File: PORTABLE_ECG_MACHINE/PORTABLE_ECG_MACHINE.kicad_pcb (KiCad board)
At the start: 2 copper layers, 25.5 x 64.8 mm, 83 parts, among them IC1 AD8232ACPZ, J1 UART, J2 AudioJack3, J3 Li-Ion 3.7 CONN, J4 USB_C_Receptacle_USB2.0, Q1 BSS138, Q2 BSS138, SW1 SW_SPDT, U1 SSD1306, U2 CP2102-GM, U3 ATmega328PB-A, U4 TC1262-33, U5 TP4056, Y1 16MHZ

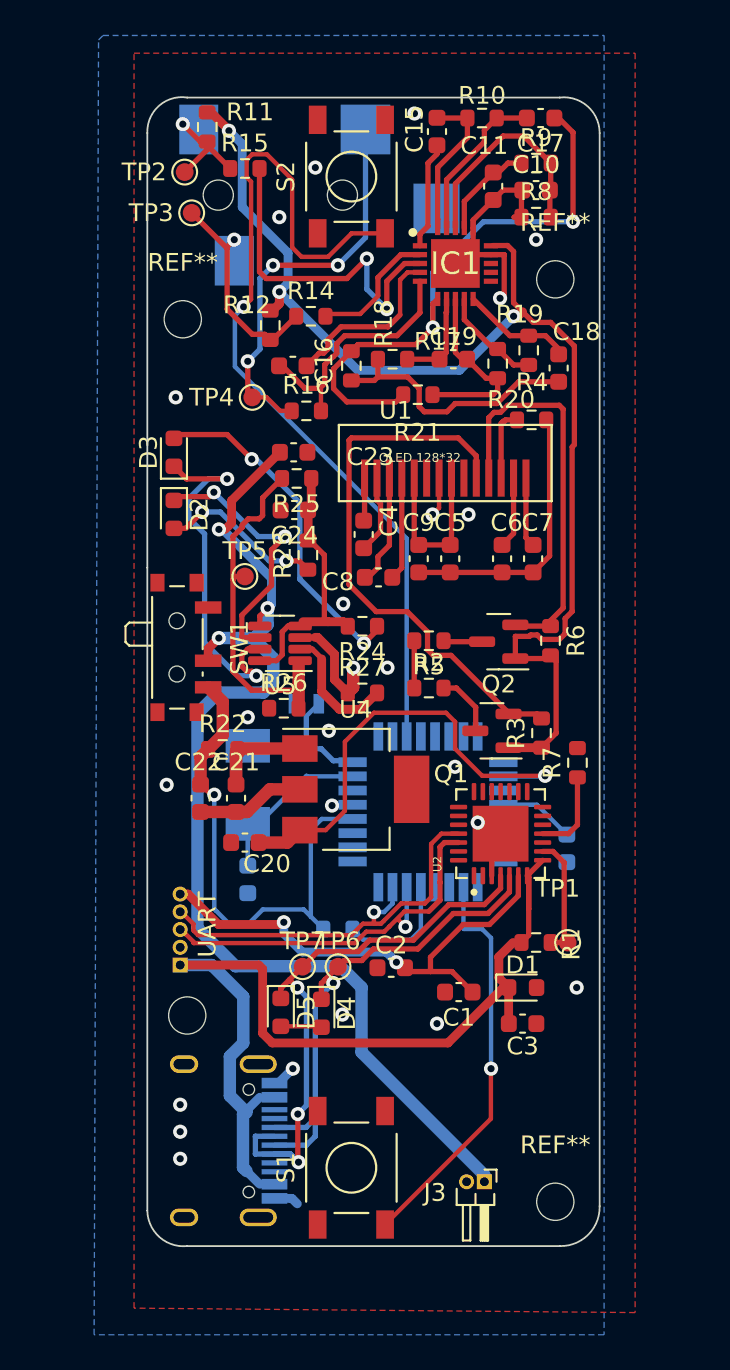
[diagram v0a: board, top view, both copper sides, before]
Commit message: F.SILK AND B.SILK -- FONT FIX | LAYOUT FIX
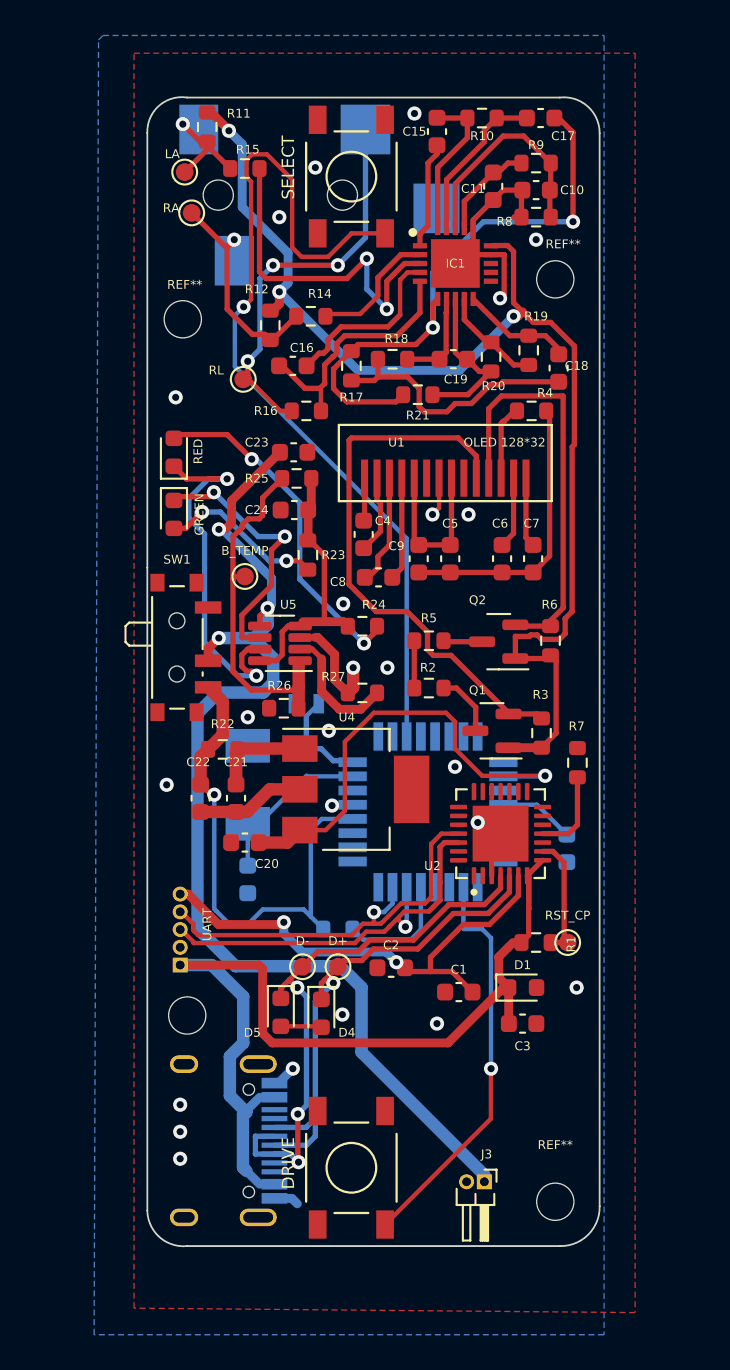
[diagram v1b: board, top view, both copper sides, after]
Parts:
- moved RL 1.14 mm to (89.4, 40.4)
- moved R20 0.53 mm to (103.4, 39.1)
- moved R4 0.51 mm to (105.7, 42.2)
- renumbered TP5 to B_TEMP, TP6 to D+, TP7 to D-, S1 to DRIVE, D2 to GREEN, TP2 to LA, TP3 to RA, D3 to RED, TP4 to RL, TP1 to RST_CP, S2 to SELECT
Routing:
- net SDA_3.3: track 22.4 -> 23.6 mm
- net /REF_OUT: track 10.5 -> 9.35 mm
- net GND: track 54.8 -> 55.3 mm
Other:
- board text added: "*"
- board text added: "+"
- board text added: "-"
- board text added: "AMIT TONY JOSEPH"
- board text added: "ARUN JYOTHISH"
- board text added: "ATMEGA328PB-A"
- board text added: "BAT 3.7"
- board text added: "BHARATH SRINIVAS"
- board text added: "GOURI KRISHNA"
- board text added: "GROUP NO. 5"
- board text added: "TEAM MEMBERS"

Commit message: CUSTOM PAD ADD | ANNOTATION CONFLICT RECTIFY
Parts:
- added J5: Conn_01x06_Male, TEST_POINT_MATRIX_6-PIN:6PIN_CONN, B.Cu at (104.9, 59.7)
- renumbered B_TEMP to B_TEMP1, D+ to D+1, D- to D-1, D4 to D2, D5 to D3, DRIVE to DRIVE1, GREEN to GREEN1, LA to LA1, R13 to R11, R11 to R12, R12 to R13, RA to RA1, RED to RED1, RL to RL1, RST_CP to RST_CP1, SELECT to SELECT1
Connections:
- U3 pad 12: unconnected-(U3-Pad12) -> Net-(U3-Pad12)
- U3 pad 13: unconnected-(U3-Pad13) -> Net-(U3-Pad13)
- U3 pad 14: unconnected-(U3-Pad14) -> Net-(U3-Pad14)
- U3 pad 15: unconnected-(U3-Pad15) -> Net-(U3-Pad15)
- U3 pad 16: unconnected-(U3-Pad16) -> Net-(U3-Pad16)
- U3 pad 17: unconnected-(U3-Pad17) -> Net-(U3-Pad17)
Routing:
- net Net-(U3-Pad13): track 0.00 -> 11.7 mm
- net Net-(U3-Pad12): track 0.00 -> 11.3 mm
- net Net-(U3-Pad15): track 0.00 -> 9.41 mm
- net Net-(U3-Pad14): track 0.00 -> 9.01 mm
- net Net-(U3-Pad17): track 0.00 -> 7.08 mm
- net Net-(U3-Pad16): track 0.00 -> 6.76 mm

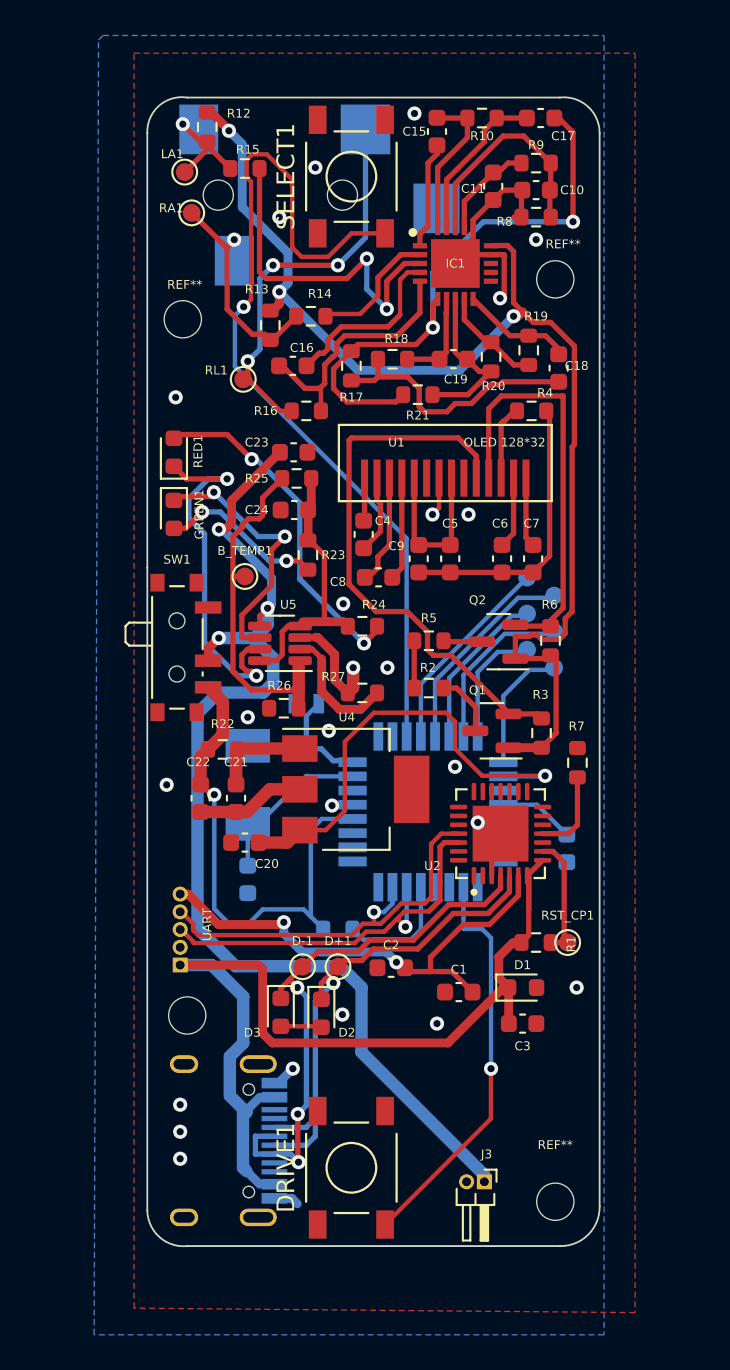
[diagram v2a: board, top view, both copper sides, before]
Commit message: conn complete | solder jumper add
pcbnew connection complete with respect to schematics, solder jumper add
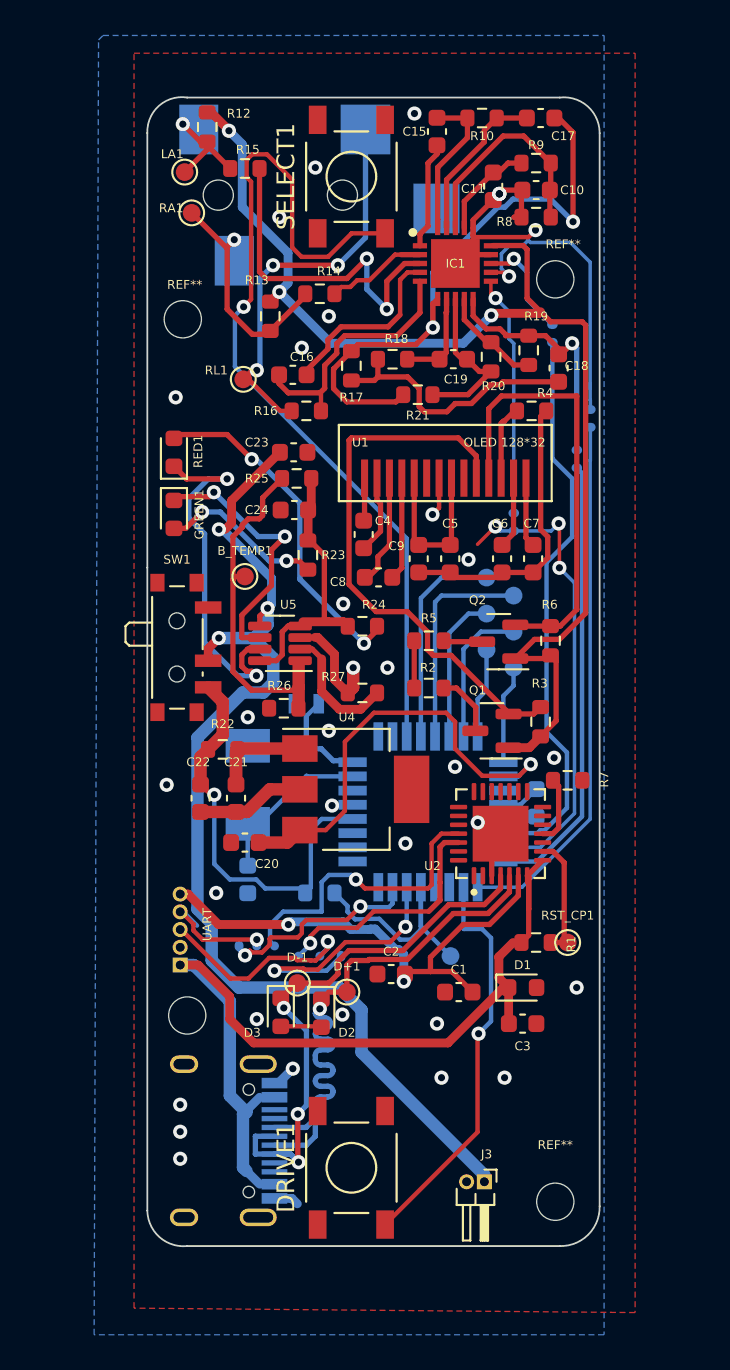
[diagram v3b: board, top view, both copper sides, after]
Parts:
- added JP1: SolderJumper_3_Open, TEST_POINT_MATRIX_6-PIN:3_PIN_SOLDER_JUMPER_SMD, B.Cu at (94.3, 70.3)
- added JP2: SolderJumper_3_Open, TEST_POINT_MATRIX_6-PIN:3_PIN_SOLDER_JUMPER_SMD, B.Cu at (89.6, 74.9)
- added JP3: LDO+, TEST_POINT_MATRIX_6-PIN:2_PIN_SMD_SOLDER_JUMPER, B.Cu at (112.8, 43.7)
- added JP4: LDO-, TEST_POINT_MATRIX_6-PIN:2_PIN_SMD_SOLDER_JUMPER, B.Cu at (108.5, 49.5)
- added JP5: OUT, TEST_POINT_MATRIX_6-PIN:2_PIN_SMD_SOLDER_JUMPER, B.Cu at (112.0, 46.0)
- added JP6: LDO+, TEST_POINT_MATRIX_6-PIN:2_PIN_SMD_SOLDER_JUMPER, B.Cu at (110.6, 38.9)
- added TP1: AT_RST#, TestPoint:TestPoint_Pad_D1.0mm, B.Cu at (101.1, 72.9)
- moved C12 3.10 mm to (105.9, 64.3)
- moved J5 2.29 mm to (102.6, 59.7)
- moved R11 2.27 mm to (93.7, 69.3)
- moved D+1 1.51 mm to (95.2, 74.9)
- moved R14 1.37 mm to (93.7, 35.6)
- moved R7 1.14 mm to (107.7, 63.0), turned to 0 degrees
- moved D-1 0.97 mm to (92.5, 74.4)
- moved R3 0.64 mm to (106.2, 59.7)
- moved R13 0.51 mm to (90.9, 36.8)
- moved C16 0.51 mm to (92.2, 40.1)
- moved C2 0.36 mm to (97.7, 73.9)
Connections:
- net Net-(C18-Pad1) renamed /OUT
- IC1 pad 11: /LDO- -> /LOD-
- IC1 pad 12: /LDO+ -> /LOD+
- J1 pad 3: /TXD -> Net-(J1-Pad3)
- J1 pad 4: /RXD -> Net-(J1-Pad4)
- U2 pad 25: /RXD -> /CP_RXD
- U2 pad 26: /TXD -> /CP_TXD
- U3 pad 22: unconnected-(U3-Pad22) -> /AT_SDN#
- U3 pad 23: unconnected-(U3-Pad23) -> /AT_LOD-
- U3 pad 24: unconnected-(U3-Pad24) -> /AT_ADC1
- U3 pad 25: unconnected-(U3-Pad25) -> /AT_LOD+
- U3 pad 30: /TXD -> /AT_RXD
- U3 pad 31: /RXD -> /AT_TXD
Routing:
- net /AT_SDN#: track 0.00 -> 32.0 mm
- net /AT_LOD+: track 0.00 -> 30.0 mm
- net /AT_LOD-: track 0.00 -> 26.8 mm, vias 0 -> 3
- net /AT_ADC1: track 0.00 -> 25.3 mm
- net /RXD: track 23.4 -> 0.00 mm, vias 1 -> 0
- net /TXD: track 23.0 -> 0.00 mm, vias 1 -> 0
- net /CP_RXD: track 0.00 -> 17.0 mm, vias 0 -> 1
- net /LOD+: track 0.00 -> 17.0 mm, vias 0 -> 1
- net /AT_RXD: track 0.00 -> 14.8 mm, vias 0 -> 2
- net /CP_TXD: track 0.00 -> 13.7 mm, vias 0 -> 1
- net /LOD-: track 0.00 -> 13.6 mm, vias 0 -> 1
- net Net-(J1-Pad3): track 0.00 -> 11.7 mm, vias 0 -> 1
- net /AT_TXD: track 0.00 -> 11.6 mm, vias 0 -> 2
- net /OUT: track 6.29 -> 14.0 mm, vias 0 -> 1
- net Net-(J1-Pad4): track 0.00 -> 6.81 mm, vias 0 -> 1
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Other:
- board text added: "MISO"
- board text added: "MOSI"
- board text added: "PB0"
- board text added: "PB1"
- board text added: "PB2"
- board text added: "SCK"

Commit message: new revision initiate
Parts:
- moved R7 1.78 mm to (107.7, 61.2), turned to 90 degrees
- moved D2 1.14 mm to (93.5, 77.2)
- moved R3 1.02 mm to (106.2, 58.7)
- moved D-1 0.76 mm to (93.2, 74.4)
- moved D3 0.38 mm to (91.5, 76.5)
- moved C19 0.16 mm to (101.1, 39.2)
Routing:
- net GND: track 58.2 -> 77.9 mm
- net VIN: track 52.8 -> 58.0 mm
- net /AT_LOD-: track 26.8 -> 24.2 mm, vias 3 -> 2
- net Net-(R7-Pad1): track 3.85 -> 4.88 mm
- net 3.3V: track 68.9 -> 68.3 mm

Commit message: git pull stash?
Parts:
- added REF**: SSD1306-128*64, user_ftprint:SSD1306-128*64, F.Cu at (91.9, 78.5)
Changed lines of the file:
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@@
     )
+  )
+  (footprint "user_ftprint:SSD1306-128*64" (layer "F.Cu")
+    (at 91.948 78.486)
+    (attr smd)
+    (fp_text reference "REF**" (at 0 -0.5 unlocked) (layer "F.SilkS")
+      (effects (font (size 1 1) (thickness 0.15)))
+    )
+    (fp_text value "SSD1306-128*64" (at 0 1 unlocked) (layer "F.Fab")
+      (effects (font (size 1 1) (thickness 0.15)))
+    )
+    (fp_text user "${REFERENCE}" (at 0 2.5 unlocked) (layer "F.Fab")
+      (effects (font (size 1 1) (thickness 0.15)))
+    )
+    (fp_line (start 14.86 6.07) (end 6 6.07) (layer "F.SilkS") (width 0.12))
+    (fp_line (start -5.96 1.77) (end 6.04 1.77) (layer "F.SilkS") (width 0.127))
+    (fp_line (start 6.04 6.07) (end -5.96 6.07) (layer "F.SilkS") (width 0.127))
+    (fp_line (start 14.87 1.77) (end 14.86 6.06) (layer "F.SilkS") (width 0.12))
+    (fp_line (start 6.04 1.77) (end 14.87 1.77) (layer "F.SilkS") (width 0.12))
+    (fp_line (start -5.96 6.07) (end -5.96 1.77) (layer "F.SilkS") (width 0.127))
+    (pad "1" smd rect (at -4.51 4.77 180) (size 0.4 2.1) (layers "F.Cu" "F.Paste" "F.Mask"))
+    (pad "2" smd rect (at -3.81 4.77 180) (size 0.4 2.1) (layers "F.Cu" "F.Paste" "F.Mask"))
+    (pad "3" smd rect (at -3.11 4.77 180) (size 0.4 2.1) (layers "F.Cu" "F.Paste" "F.Mask"))
+    (pad "4" smd rect (at -2.41 4.77 180) (size 0.4 2.1) (layers "F.Cu" "F.Paste" "F.Mask"))
+    (pad "5" smd rect (at -1.71 4.77 180) (size 0.4 2.1) (layers "F.Cu" "F.Paste" "F.Mask"))
+    (pad "6" smd rect (at -1.01 4.77 180) (size 0.4 2.1) (layers "F.Cu" "F.Paste" "F.Mask"))
+    (pad "7" smd rect (at -0.31 4.77 180) (size 0.4 2.1) (layers "F.Cu" "F.Paste" "F.Mask"))
+    (pad "8" smd rect (at 0.39 4.77 180) (size 0.4 2.1) (layers "F.Cu" "F.Paste" "F.Mask"))
+    (pad "9" smd rect (at 1.09 4.77 180) (size 0.4 2.1) (layers "F.Cu" "F.Paste" "F.Mask"))
+    (pad "10" smd rect (at 1.79 4.77 180) (size 0.4 2.1) (layers "F.Cu" "F.Paste" "F.Mask"))
+    (pad "11" smd rect (at 2.49 4.77 180) (size 0.4 2.1) (layers "F.Cu" "F.Paste" "F.Mask"))
+    (pad "12" smd rect (at 3.19 4.77 180) (size 0.4 2.1) (layers "F.Cu" "F.Paste" "F.Mask"))
+    (pad "13" smd rect (at 3.89 4.77 180) (size 0.4 2.1) (layers "F.Cu" "F.Paste" "F.Mask"))
+    (pad "14" smd rect (at 4.59 4.77 180) (size 0.4 2.1) (layers "F.Cu" "F.Paste" "F.Mask"))
+    (pad "16" smd rect (at 5.25 4.78 180) (size 0.4 2.1) (layers "F.Cu" "F.Paste" "F.Mask"))
+    (pad "17" smd rect (at 5.86 4.78 180) (size 0.4 2.1) (layers "F.Cu" "F.Paste" "F.Mask"))
+    (pad "18" smd rect (at 6.54 4.78 180) (size 0.4 2.1) (layers "F.Cu" "F.Paste" "F.Mask"))
+    (pad "19" smd rect (at 7.21 4.79 180) (size 0.4 2.1) (layers "F.Cu" "F.Paste" "F.Mask"))
+    (pad "20" smd rect (at 7.88 4.78 180) (size 0.4 2.1) (layers "F.Cu" "F.Paste" "F.Mask"))
+    (pad "21" smd rect (at 8.54 4.77 180) (size 0.4 2.1) (layers "F.Cu" "F.Paste" "F.Mask"))
+    (pad "22" smd rect (at 9.17 4.78 180) (size 0.4 2.1) (layers "F.Cu" "F.Paste" "F.Mask"))
+    (pad "23" smd rect (at 9.83 4.78 180) (size 0.4 2.1) (layers "F.Cu" "F.Paste" "F.Mask"))
+    (pad "24" smd rect (at 9.83 4.78 180) (size 0.4 2.1) (layers "F.Cu" "F.Paste" "F.Mask"))
+    (pad "25" smd rect (at 10.49 4.78 180) (size 0.4 2.1) (layers "F.Cu" "F.Paste" "F.Mask"))
+    (pad "26" smd rect (at 11.13 4.79 180) (size 0.4 2.1) (layers "F.Cu" "F.Paste" "F.Mask"))
+    (pad "27" smd rect (at 11.78 4.79 180) (size 0.4 2.1) (layers "F.Cu" "F.Paste" "F.Mask"))
+    (pad "28" smd rect (at 12.45 4.78 180) (size 0.4 2.1) (layers "F.Cu" "F.Paste" "F.Mask"))
+    (pad "29" smd rect (at 13.15 4.79 180) (size 0.4 2.1) (layers "F.Cu" "F.Paste" "F.Mask"))
+    (pad "30" smd rect (at 13.83 4.79 180) (size 0.4 2.1) (layers "F.Cu" "F.Paste" "F.Mask"))
   )
   (footprint "Button_Switch_SMD:SW_SPDT_PCM12" (layer "F.Cu")
